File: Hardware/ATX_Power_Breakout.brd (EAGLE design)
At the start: 34.3 x 33.7 mm, 22 parts

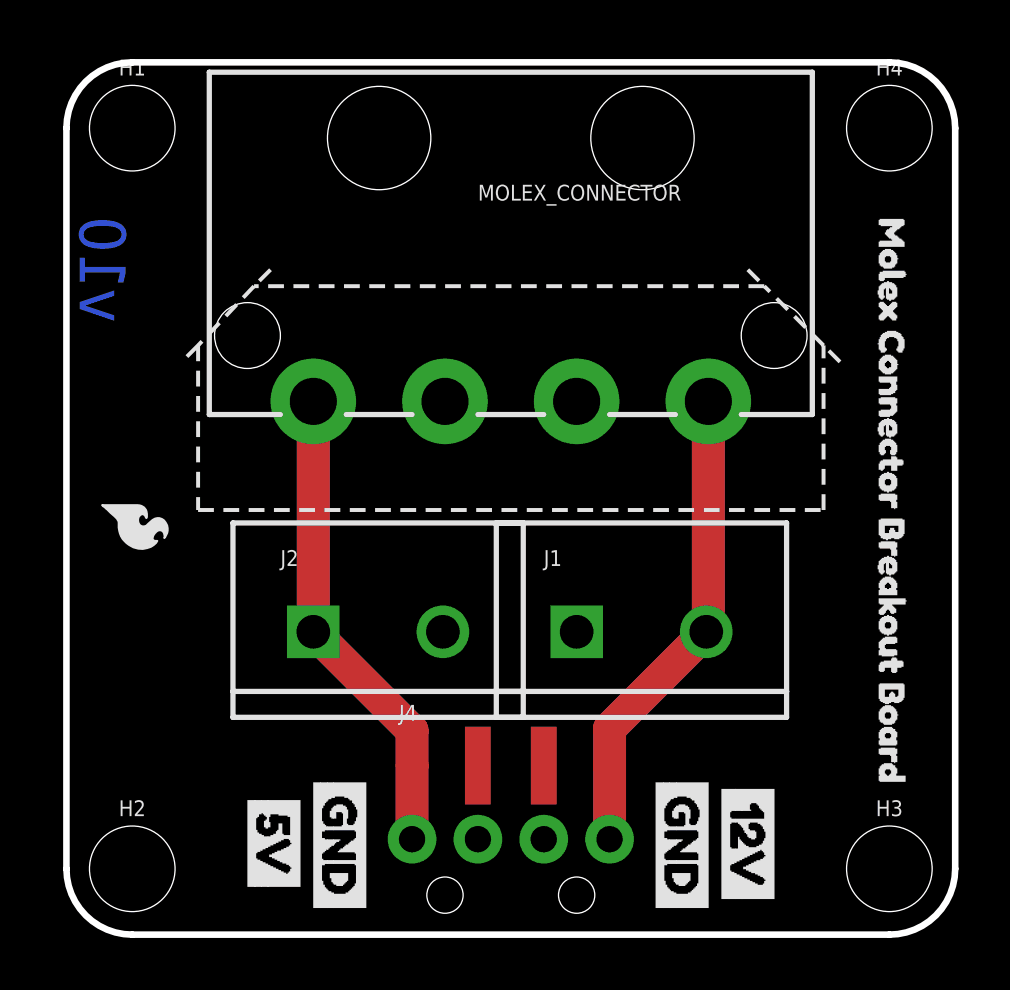
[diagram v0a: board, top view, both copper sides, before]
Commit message: Rename Board and Files
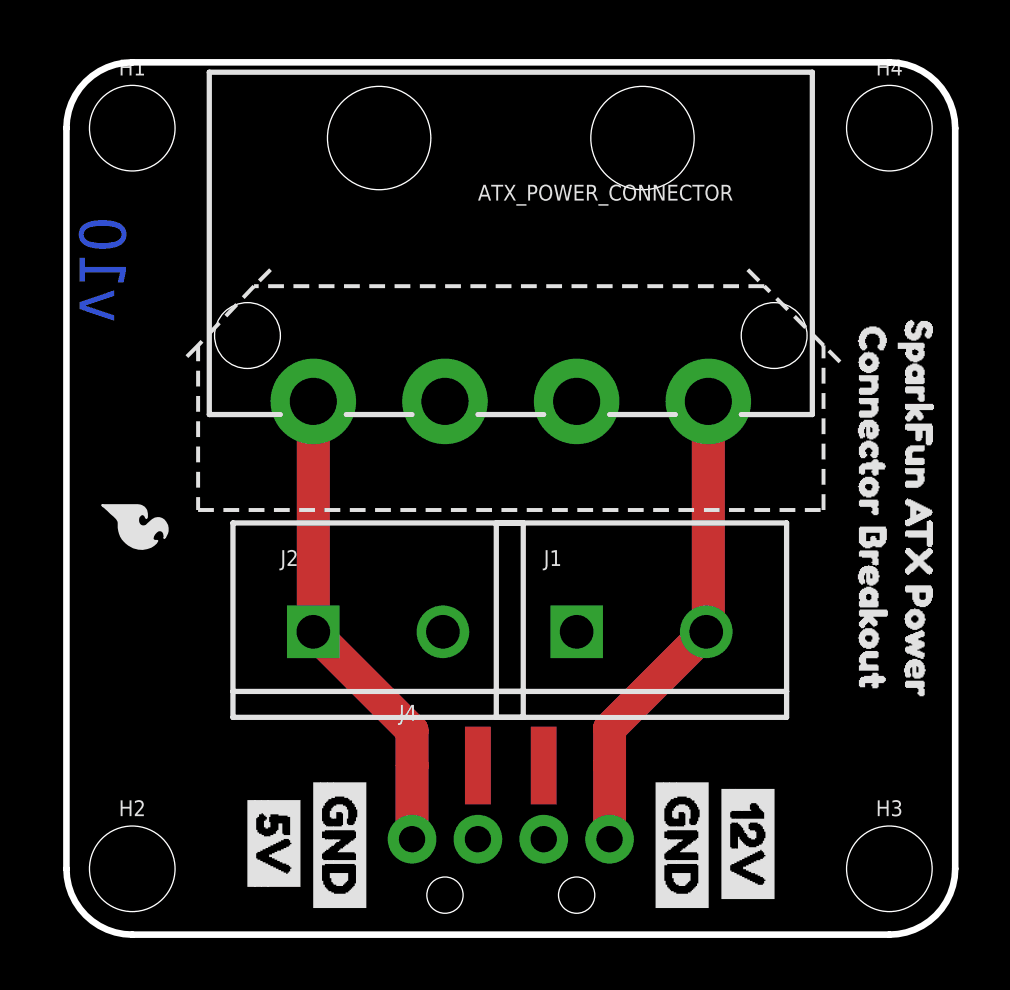
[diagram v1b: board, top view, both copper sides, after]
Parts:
- added U$10: (no value), buzzard_labels (2):CONNECTOR_BREAKOUT0
- U$9: device MolexConnectorBreakout2:MOLEX_CONNECTOR_BREAKOUT_BOARD0 -> buzzard_labels (3):SPARKFUN_ATX_POWER0
- moved U$9 4.07 mm to (32.9, 24.6)
- renumbered MOLEX_CONNECTOR to ATX_POWER_CONNECTOR
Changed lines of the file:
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@@
 <elements>
 <element name="FRAME1" library="SparkFun-Aesthetics" package="CREATIVE_COMMONS" value="FRAME-LETTER" x="-17.78" y="-23.495"/>
-<element name="MOLEX_CONNECTOR" library="SparkFun-Retired" package="COMPUTER-PERIPHERAL-POWER-RA" value="COMPUTER_PERIPHERAL_POWERRA" x="17.145" y="23.114" smashed="yes">
+<element name="ATX_POWER_CONNECTOR" library="SparkFun-Retired" package="COMPUTER-PERIPHERAL-POWER-RA" value="COMPUTER_PERIPHERAL_POWERRA" x="17.145" y="23.114" smashed="yes">
 <attribute name="NAME" x="15.875" y="28.321" size="0.6096" layer="25" font="vector" ratio="15"/>
 <attribute name="VALUE" x="15.875" y="24.892" size="0.6096" layer="27" font="vector" ratio="15"/>
@@
 <element name="U$7" library="GND Buzzard" package="GND0" value="" x="10.541" y="0.381" rot="MR90"/>
 <element name="U$8" library="5V Buzzard" package="5V0" value="" x="8.001" y="1.143" rot="MR90"/>
-<element name="U$9" library="MolexConnectorBreakout2" package="MOLEX_CONNECTOR_BREAKOUT_BOARD0" value="" x="31.877" y="28.575" rot="R270"/>
+<element name="U$9" library="buzzard_labels (3)" package="SPARKFUN_ATX_POWER0" value="" x="32.893" y="24.638" rot="R270"/>
+<element name="U$10" library="buzzard_labels (2)" package="CONNECTOR_BREAKOUT0" value="" x="31.115" y="24.384" rot="R270"/>
 </elements>
 <signals>
 <signal name="GND">
-<contactref element="MOLEX_CONNECTOR" pad="GND@1"/>
+<contactref element="ATX_POWER_CONNECTOR" pad="GND@1"/>
 <contactref element="J2" pad="2"/>
 <contactref element="J3" pad="2"/>
 <contactref element="J4" pad="2"/>
-<contactref element="MOLEX_CONNECTOR" pad="GND@2"/>
+<contactref element="ATX_POWER_CONNECTOR" pad="GND@2"/>
 <contactref element="J1" pad="1"/>
 <contactref element="J4" pad="3"/>
@@
 </signal>
 <signal name="5V">
-<contactref element="MOLEX_CONNECTOR" pad="5V"/>
+<contactref element="ATX_POWER_CONNECTOR" pad="5V"/>
 <contactref element="J2" pad="1"/>
 <contactref element="J3" pad="1"/>
@@
 </signal>
 <signal name="12V">
-<contactref element="MOLEX_CONNECTOR" pad="12V"/>
+<contactref element="ATX_POWER_CONNECTOR" pad="12V"/>
 <contactref element="J1" pad="2"/>
 <contactref element="J3" pad="4"/>
